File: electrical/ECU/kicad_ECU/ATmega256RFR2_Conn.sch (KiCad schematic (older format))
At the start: 54 parts

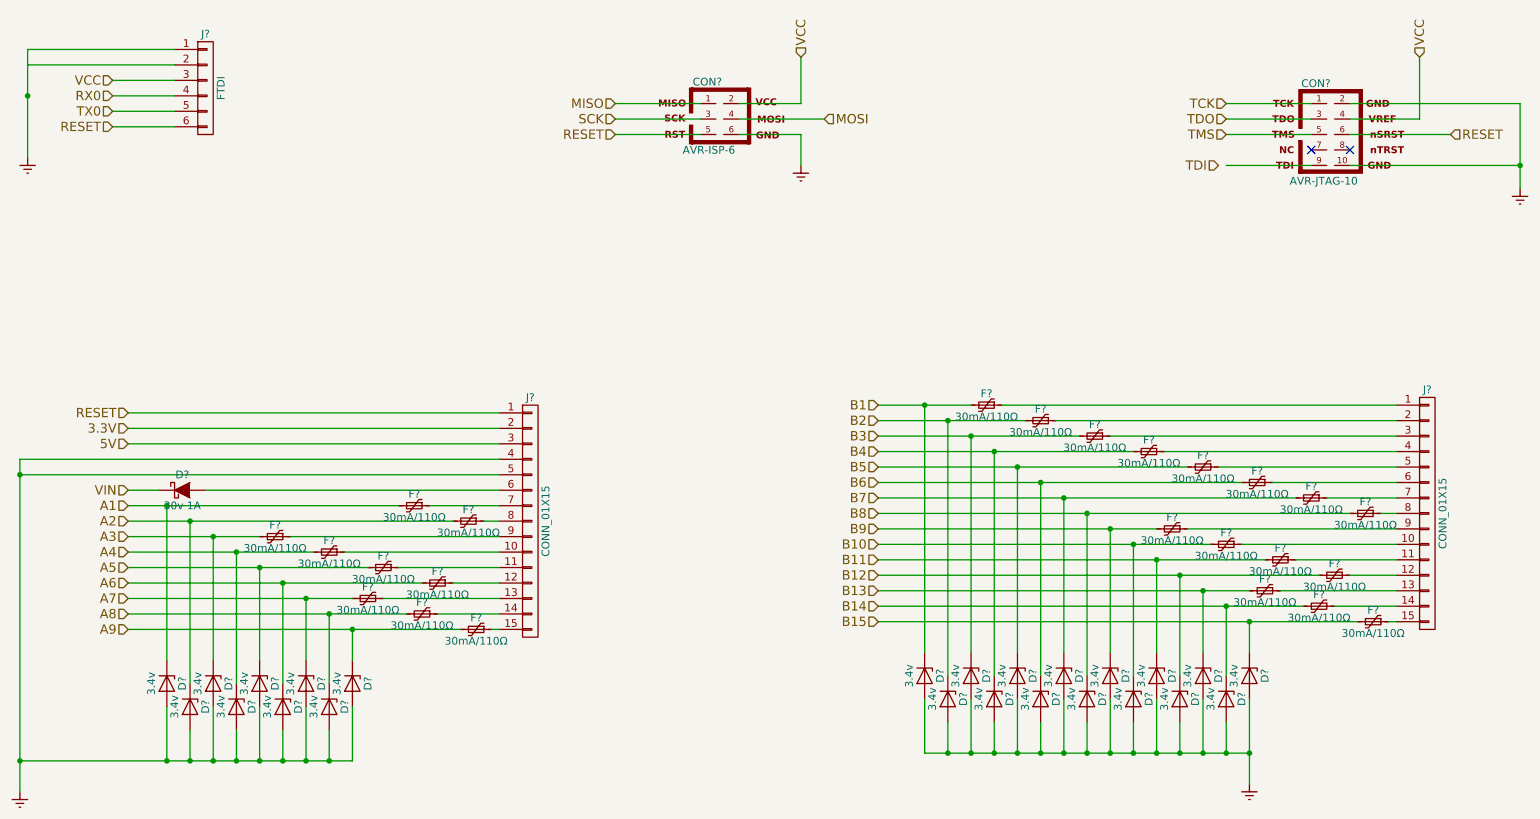
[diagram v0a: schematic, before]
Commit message: fixed some naming errors and initial round of double checking
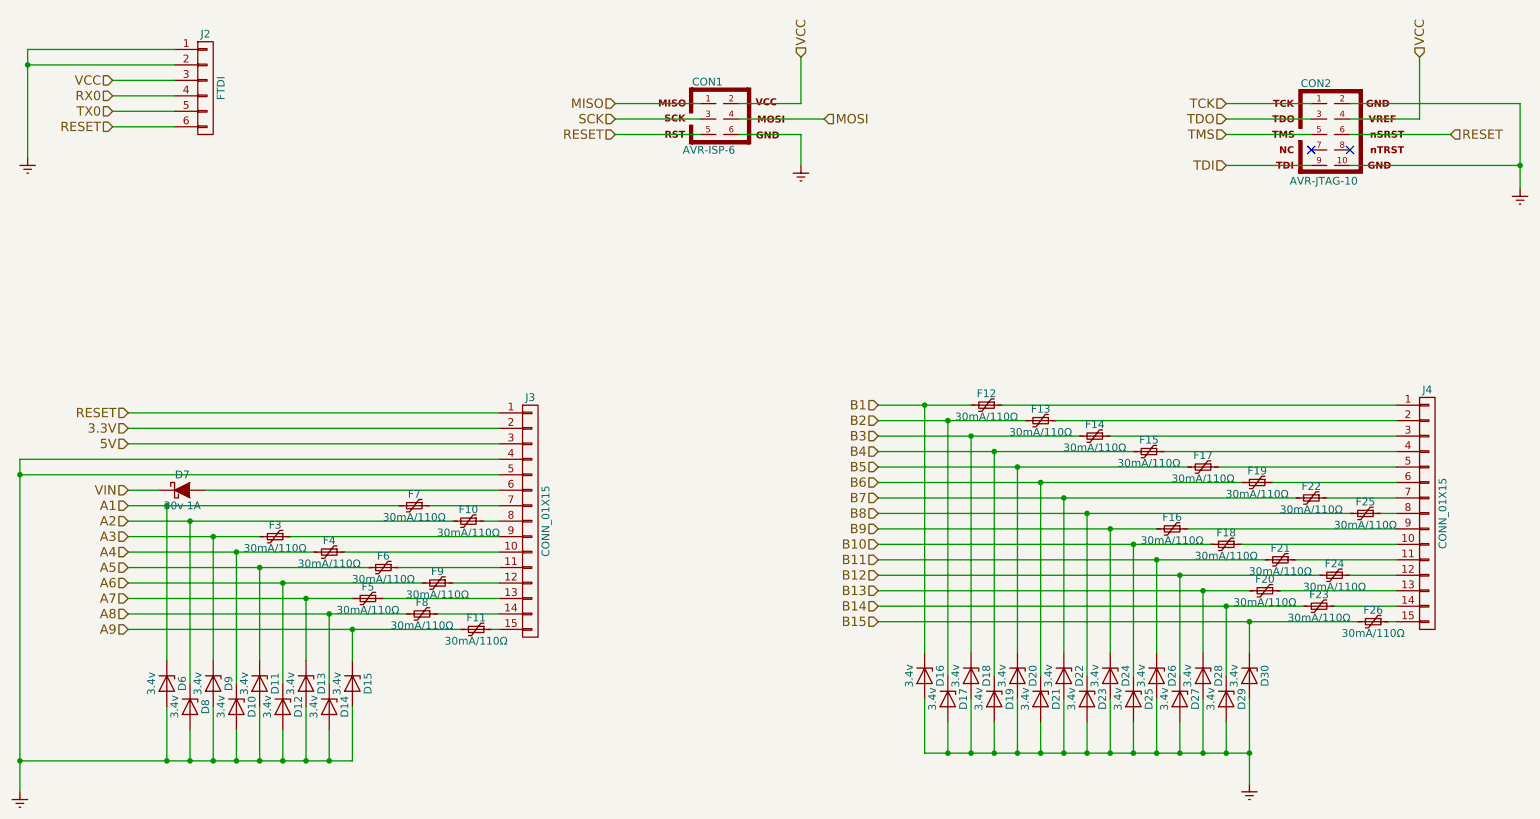
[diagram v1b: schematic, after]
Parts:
- gave numbers to parts that had none: 54
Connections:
- net Earth: now also J2.2 (P2)
- net TDI: now also CON2.9
